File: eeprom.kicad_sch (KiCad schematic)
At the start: 4 parts

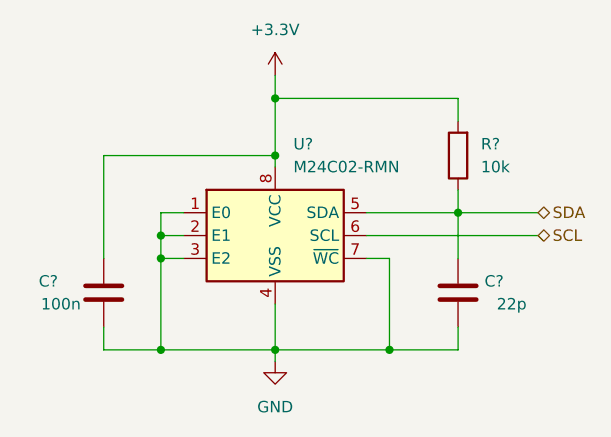
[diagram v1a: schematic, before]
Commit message: added power loss detection, preparing for new pcb layout
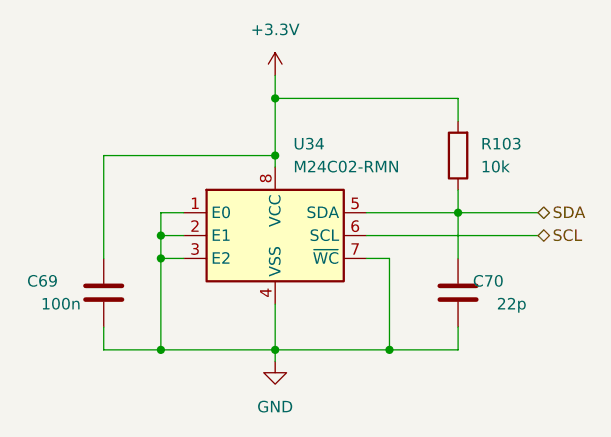
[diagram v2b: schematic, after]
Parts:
- gave numbers to parts that had none: 4
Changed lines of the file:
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@@
   (symbol (lib_id "Memory_EEPROM:M24C02-RMN") (at 139.7 92.71 0) (unit 1)
     (in_bom yes) (on_board yes) (fields_autoplaced)
-    (property "Reference" "U?" (id 0) (at 141.7194 82.55 0)
+    (property "Reference" "U34" (id 0) (at 141.7194 82.55 0)
       (effects (font (size 1.27 1.27)) (justify left))
     )
@@
   (symbol (lib_id "Device:C") (at 160.02 99.06 0) (mirror y) (unit 1)
     (in_bom yes) (on_board yes)
-    (property "Reference" "C?" (id 0) (at 165.1 97.79 0)
+    (property "Reference" "C70" (id 0) (at 165.1 97.79 0)
       (effects (font (size 1.27 1.27)) (justify left))
     )
@@
   (symbol (lib_id "Device:R") (at 160.02 83.82 180) (unit 1)
     (in_bom yes) (on_board yes) (fields_autoplaced)
-    (property "Reference" "R?" (id 0) (at 162.56 82.5499 0)
+    (property "Reference" "R103" (id 0) (at 162.56 82.5499 0)
       (effects (font (size 1.27 1.27)) (justify right))
     )
@@
   (symbol (lib_id "power:+3.3V") (at 139.7 74.93 0) (unit 1)
     (in_bom yes) (on_board yes) (fields_autoplaced)
-    (property "Reference" "#PWR?" (id 0) (at 139.7 78.74 0)
+    (property "Reference" "#PWR0161" (id 0) (at 139.7 78.74 0)
       (effects (font (size 1.27 1.27)) hide)
     )
@@
   (symbol (lib_id "power:GND") (at 139.7 106.68 0) (unit 1)
     (in_bom yes) (on_board yes) (fields_autoplaced)
-    (property "Reference" "#PWR?" (id 0) (at 139.7 113.03 0)
+    (property "Reference" "#PWR0154" (id 0) (at 139.7 113.03 0)
       (effects (font (size 1.27 1.27)) hide)
     )
@@
   (symbol (lib_id "Device:C") (at 120.65 99.06 0) (mirror y) (unit 1)
     (in_bom yes) (on_board yes)
-    (property "Reference" "C?" (id 0) (at 115.57 97.79 0)
+    (property "Reference" "C69" (id 0) (at 115.57 97.79 0)
       (effects (font (size 1.27 1.27)) (justify left))
     )

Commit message: pcb is in progress, finishing H-bridge layout
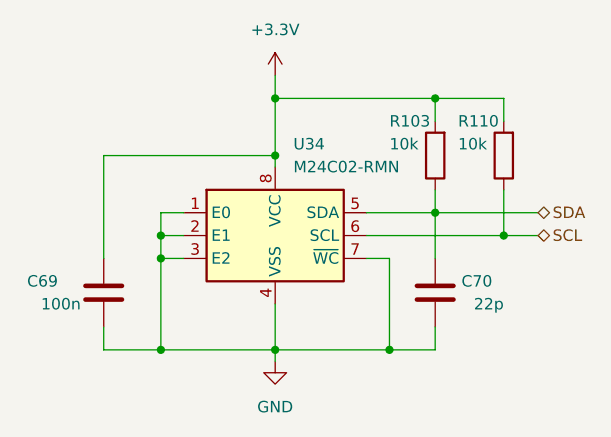
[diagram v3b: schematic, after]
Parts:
- added R110: 10k, Resistor_SMD:R_0603_1608Metric_Pad0.98x0.95mm_HandSolder, symbol Device:R
- C69, C70: footprint Capacitor_SMD:C_0603_1608Metric -> Capacitor_SMD:C_0603_1608Metric_Pad1.08x0.95mm_HandSolder
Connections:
- net +3V3: now also R110.2
- net SCL: now also R110.1
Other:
- moved on the sheet: C70, R103
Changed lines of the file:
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@@
   (junction (at 127 105.41) (diameter 0) (color 0 0 0 0)
   )
+  (junction (at 165.1 92.71) (diameter 0) (color 0 0 0 0)
+  )
+  (junction (at 139.7 105.41) (diameter 0) (color 0 0 0 0)
+  )
+  (junction (at 157.48 77.47) (diameter 0) (color 0 0 0 0)
+  )
+  (junction (at 139.7 77.47) (diameter 0) (color 0 0 0 0)
+  )
+  (junction (at 157.48 90.17) (diameter 0) (color 0 0 0 0)
+  )
+  (junction (at 127 92.71) (diameter 0) (color 0 0 0 0)
+  )
   (junction (at 152.4 105.41) (diameter 0) (color 0 0 0 0)
   )
-  (junction (at 139.7 77.47) (diameter 0) (color 0 0 0 0)
-  )
-  (junction (at 139.7 105.41) (diameter 0) (color 0 0 0 0)
-  )
-  (junction (at 160.02 90.17) (diameter 0) (color 0 0 0 0)
-  )
-  (junction (at 127 92.71) (diameter 0) (color 0 0 0 0)
-  )
   (junction (at 139.7 83.82) (diameter 0) (color 0 0 0 0)
   )
   (junction (at 127 95.25) (diameter 0) (color 0 0 0 0)
   )
+  (wire (pts (xy 139.7 77.47) (xy 139.7 83.82))
+    (stroke (width 0) (type default) (color 0 0 0 0))
+  )
+  (wire (pts (xy 157.48 105.41) (xy 152.4 105.41))
+    (stroke (width 0) (type default) (color 0 0 0 0))
+  )
+  (wire (pts (xy 165.1 87.63) (xy 165.1 92.71))
+    (stroke (width 0) (type default) (color 0 0 0 0))
+  )
+  (wire (pts (xy 120.65 102.87) (xy 120.65 105.41))
+    (stroke (width 0) (type default) (color 0 0 0 0))
+  )
+  (wire (pts (xy 165.1 92.71) (xy 168.91 92.71))
+    (stroke (width 0) (type default) (color 0 0 0 0))
+  )
+  (wire (pts (xy 127 105.41) (xy 139.7 105.41))
+    (stroke (width 0) (type default) (color 0 0 0 0))
+  )
+  (wire (pts (xy 120.65 95.25) (xy 120.65 83.82))
+    (stroke (width 0) (type default) (color 0 0 0 0))
+  )
+  (wire (pts (xy 149.86 95.25) (xy 152.4 95.25))
+    (stroke (width 0) (type default) (color 0 0 0 0))
+  )
+  (wire (pts (xy 120.65 105.41) (xy 127 105.41))
+    (stroke (width 0) (type default) (color 0 0 0 0))
+  )
   (wire (pts (xy 139.7 74.93) (xy 139.7 77.47))
     (stroke (width 0) (type default) (color 0 0 0 0))
   )
-  (wire (pts (xy 120.65 102.87) (xy 120.65 105.41))
-    (stroke (width 0) (type default) (color 0 0 0 0))
-  )
-  (wire (pts (xy 127 105.41) (xy 139.7 105.41))
-    (stroke (width 0) (type default) (color 0 0 0 0))
-  )
-  (wire (pts (xy 120.65 95.25) (xy 120.65 83.82))
-    (stroke (width 0) (type default) (color 0 0 0 0))
-  )
-  (wire (pts (xy 149.86 95.25) (xy 152.4 95.25))
-    (stroke (width 0) (type default) (color 0 0 0 0))
-  )
-  (wire (pts (xy 120.65 105.41) (xy 127 105.41))
-    (stroke (width 0) (type default) (color 0 0 0 0))
-  )
-  (wire (pts (xy 139.7 77.47) (xy 160.02 77.47))
-    (stroke (width 0) (type default) (color 0 0 0 0))
-  )
-  (wire (pts (xy 139.7 77.47) (xy 139.7 83.82))
-    (stroke (width 0) (type default) (color 0 0 0 0))
-  )
-  (wire (pts (xy 160.02 90.17) (xy 160.02 95.25))
-    (stroke (width 0) (type default) (color 0 0 0 0))
-  )
-  (wire (pts (xy 160.02 80.01) (xy 160.02 77.47))
+  (wire (pts (xy 157.48 90.17) (xy 157.48 95.25))
     (stroke (width 0) (type default) (color 0 0 0 0))
   )
@@
     (stroke (width 0) (type default) (color 0 0 0 0))
   )
-  (wire (pts (xy 149.86 92.71) (xy 168.91 92.71))
+  (wire (pts (xy 157.48 77.47) (xy 157.48 80.01))
+    (stroke (width 0) (type default) (color 0 0 0 0))
+  )
+  (wire (pts (xy 149.86 92.71) (xy 165.1 92.71))
+    (stroke (width 0) (type default) (color 0 0 0 0))
+  )
+  (wire (pts (xy 165.1 77.47) (xy 165.1 80.01))
+    (stroke (width 0) (type default) (color 0 0 0 0))
+  )
+  (wire (pts (xy 157.48 102.87) (xy 157.48 105.41))
     (stroke (width 0) (type default) (color 0 0 0 0))
   )
@@
     (stroke (width 0) (type default) (color 0 0 0 0))
   )
+  (wire (pts (xy 157.48 77.47) (xy 165.1 77.47))
+    (stroke (width 0) (type default) (color 0 0 0 0))
+  )
   (wire (pts (xy 127 92.71) (xy 127 95.25))
     (stroke (width 0) (type default) (color 0 0 0 0))
   )
-  (wire (pts (xy 160.02 90.17) (xy 168.91 90.17))
-    (stroke (width 0) (type default) (color 0 0 0 0))
-  )
-  (wire (pts (xy 149.86 90.17) (xy 160.02 90.17))
+  (wire (pts (xy 157.48 90.17) (xy 168.91 90.17))
+    (stroke (width 0) (type default) (color 0 0 0 0))
+  )
+  (wire (pts (xy 149.86 90.17) (xy 157.48 90.17))
     (stroke (width 0) (type default) (color 0 0 0 0))
   )
@@
     (stroke (width 0) (type default) (color 0 0 0 0))
   )
+  (wire (pts (xy 139.7 77.47) (xy 157.48 77.47))
+    (stroke (width 0) (type default) (color 0 0 0 0))
+  )
+  (wire (pts (xy 157.48 87.63) (xy 157.48 90.17))
+    (stroke (width 0) (type default) (color 0 0 0 0))
+  )
   (wire (pts (xy 127 95.25) (xy 129.54 95.25))
     (stroke (width 0) (type default) (color 0 0 0 0))
   )
-  (wire (pts (xy 160.02 87.63) (xy 160.02 90.17))
-    (stroke (width 0) (type default) (color 0 0 0 0))
-  )
   (wire (pts (xy 120.65 83.82) (xy 139.7 83.82))
-    (stroke (width 0) (type default) (color 0 0 0 0))
-  )
-  (wire (pts (xy 160.02 102.87) (xy 160.02 105.41))
-    (stroke (width 0) (type default) (color 0 0 0 0))
-  )
-  (wire (pts (xy 152.4 105.41) (xy 160.02 105.41))
     (stroke (width 0) (type default) (color 0 0 0 0))
   )
@@
   (hierarchical_label "SCL" (shape bidirectional) (at 168.91 92.71 0)
     (effects (font (size 1.27 1.27)) (justify left))
+  )
+  (symbol (lib_id "Device:R") (at 165.1 83.82 180) (unit 1)
+    (in_bom yes) (on_board yes)
+    (property "Reference" "R110" (id 0) (at 160.02 80.01 0)
+      (effects (font (size 1.27 1.27)) (justify right))
+    )
+    (property "Value" "10k" (id 1) (at 160.02 82.55 0)
+      (effects (font (size 1.27 1.27)) (justify right))
+    )
+    (property "Footprint" "Resistor_SMD:R_0603_1608Metric_Pad0.98x0.95mm_HandSolder" (id 2) (at 166.878 83.82 90)
+      (effects (font (size 1.27 1.27)) hide)
+    )
+    (property "Datasheet" "~" (id 3) (at 165.1 83.82 0)
+      (effects (font (size 1.27 1.27)) hide)
+    )
+    (pin "1")
+    (pin "2")
   )
   (symbol (lib_id "Memory_EEPROM:M24C02-RMN") (at 139.7 92.71 0) (unit 1)
@@
     (pin "8")
   )
-  (symbol (lib_id "Device:C") (at 160.02 99.06 0) (mirror y) (unit 1)
-    (in_bom yes) (on_board yes)
-    (property "Reference" "C70" (id 0) (at 165.1 97.79 0)
-      (effects (font (size 1.27 1.27)) (justify left))
-    )
-    (property "Value" "22p" (id 1) (at 167.64 100.33 0)
-      (effects (font (size 1.27 1.27)) (justify left))
-    )
-    (property "Footprint" "Capacitor_SMD:C_0603_1608Metric" (id 2) (at 159.0548 102.87 0)
-      (effects (font (size 1.27 1.27)) hide)
-    )
-    (property "Datasheet" "~" (id 3) (at 160.02 99.06 0)
-      (effects (font (size 1.27 1.27)) hide)
-    )
-    (pin "1")
-    (pin "2")
-  )
-  (symbol (lib_id "Device:R") (at 160.02 83.82 180) (unit 1)
-    (in_bom yes) (on_board yes) (fields_autoplaced)
-    (property "Reference" "R103" (id 0) (at 162.56 82.5499 0)
-      (effects (font (size 1.27 1.27)) (justify right))
-    )
-    (property "Value" "10k" (id 1) (at 162.56 85.0899 0)
-      (effects (font (size 1.27 1.27)) (justify right))
-    )
-    (property "Footprint" "Resistor_SMD:R_0603_1608Metric_Pad0.98x0.95mm_HandSolder" (id 2) (at 161.798 83.82 90)
-      (effects (font (size 1.27 1.27)) hide)
-    )
-    (property "Datasheet" "~" (id 3) (at 160.02 83.82 0)
+  (symbol (lib_id "Device:C") (at 157.48 99.06 0) (mirror y) (unit 1)
+    (in_bom yes) (on_board yes)
+    (property "Reference" "C70" (id 0) (at 163.83 97.79 0)
+      (effects (font (size 1.27 1.27)) (justify left))
+    )
+    (property "Value" "22p" (id 1) (at 165.1 100.33 0)
+      (effects (font (size 1.27 1.27)) (justify left))
+    )
+    (property "Footprint" "Capacitor_SMD:C_0603_1608Metric_Pad1.08x0.95mm_HandSolder" (id 2) (at 156.5148 102.87 0)
+      (effects (font (size 1.27 1.27)) hide)
+    )
+    (property "Datasheet" "~" (id 3) (at 157.48 99.06 0)
+      (effects (font (size 1.27 1.27)) hide)
+    )
+    (pin "1")
+    (pin "2")
+  )
+  (symbol (lib_id "Device:R") (at 157.48 83.82 180) (unit 1)
+    (in_bom yes) (on_board yes)
+    (property "Reference" "R103" (id 0) (at 152.4 80.01 0)
+      (effects (font (size 1.27 1.27)) (justify right))
+    )
+    (property "Value" "10k" (id 1) (at 152.4 82.55 0)
+      (effects (font (size 1.27 1.27)) (justify right))
+    )
+    (property "Footprint" "Resistor_SMD:R_0603_1608Metric_Pad0.98x0.95mm_HandSolder" (id 2) (at 159.258 83.82 90)
+      (effects (font (size 1.27 1.27)) hide)
+    )
+    (property "Datasheet" "~" (id 3) (at 157.48 83.82 0)
       (effects (font (size 1.27 1.27)) hide)
     )
@@
       (effects (font (size 1.27 1.27)) (justify left))
     )
-    (property "Footprint" "Capacitor_SMD:C_0603_1608Metric" (id 2) (at 119.6848 102.87 0)
-      (effects (font (size 1.27 1.27)) hide)
-    )
+    (property "Footprint" "Capacitor_SMD:C_0603_1608Metric_Pad1.08x0.95mm_HandSolder" (id 2) (at 119.6848 102.87 0)
+      (effects (font (size 1.27 1.27)) hide)
+    )

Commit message: v2.1 finished
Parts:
- added C77: 22p, Capacitor_SMD:C_0603_1608Metric_Pad1.08x0.95mm_HandSolder, symbol Device:C
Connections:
- net GND: now also C77.2
- net SCL: now also C77.1
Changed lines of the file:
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@@
   (junction (at 152.4 105.41) (diameter 0) (color 0 0 0 0)
+  )
+  (junction (at 157.48 105.41) (diameter 0) (color 0 0 0 0)
   )
   (junction (at 139.7 83.82) (diameter 0) (color 0 0 0 0)
@@
     (stroke (width 0) (type default) (color 0 0 0 0))
   )
+  (wire (pts (xy 157.48 105.41) (xy 165.1 105.41))
+    (stroke (width 0) (type default) (color 0 0 0 0))
+  )
+  (wire (pts (xy 165.1 92.71) (xy 165.1 95.25))
+    (stroke (width 0) (type default) (color 0 0 0 0))
+  )
   (wire (pts (xy 127 92.71) (xy 127 95.25))
     (stroke (width 0) (type default) (color 0 0 0 0))
@@
   )
   (wire (pts (xy 127 90.17) (xy 127 92.71))
+    (stroke (width 0) (type default) (color 0 0 0 0))
+  )
+  (wire (pts (xy 165.1 105.41) (xy 165.1 102.87))
     (stroke (width 0) (type default) (color 0 0 0 0))
   )
@@
   (hierarchical_label "SCL" (shape bidirectional) (at 168.91 92.71 0)
     (effects (font (size 1.27 1.27)) (justify left))
+  )
+  (symbol (lib_id "Device:C") (at 165.1 99.06 0) (mirror y) (unit 1)
+    (in_bom yes) (on_board yes)
+    (property "Reference" "C77" (id 0) (at 166.37 97.79 90)
+      (effects (font (size 1.27 1.27)) (justify left))
+    )
+    (property "Value" "22p" (id 1) (at 166.37 104.14 90)
+      (effects (font (size 1.27 1.27)) (justify left))
+    )
+    (property "Footprint" "Capacitor_SMD:C_0603_1608Metric_Pad1.08x0.95mm_HandSolder" (id 2) (at 164.1348 102.87 0)
+      (effects (font (size 1.27 1.27)) hide)
+    )
+    (property "Datasheet" "~" (id 3) (at 165.1 99.06 0)
+      (effects (font (size 1.27 1.27)) hide)
+    )
+    (pin "1")
+    (pin "2")
   )
   (symbol (lib_id "Device:R") (at 165.1 83.82 180) (unit 1)
@@
   (symbol (lib_id "Device:C") (at 157.48 99.06 0) (mirror y) (unit 1)
     (in_bom yes) (on_board yes)
-    (property "Reference" "C70" (id 0) (at 163.83 97.79 0)
+    (property "Reference" "C70" (id 0) (at 158.75 97.79 90)
       (effects (font (size 1.27 1.27)) (justify left))
     )
-    (property "Value" "22p" (id 1) (at 165.1 100.33 0)
+    (property "Value" "22p" (id 1) (at 158.75 104.14 90)
       (effects (font (size 1.27 1.27)) (justify left))
     )
